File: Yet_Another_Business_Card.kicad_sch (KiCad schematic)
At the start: 415 parts, among them U1 STM32F103C8Tx

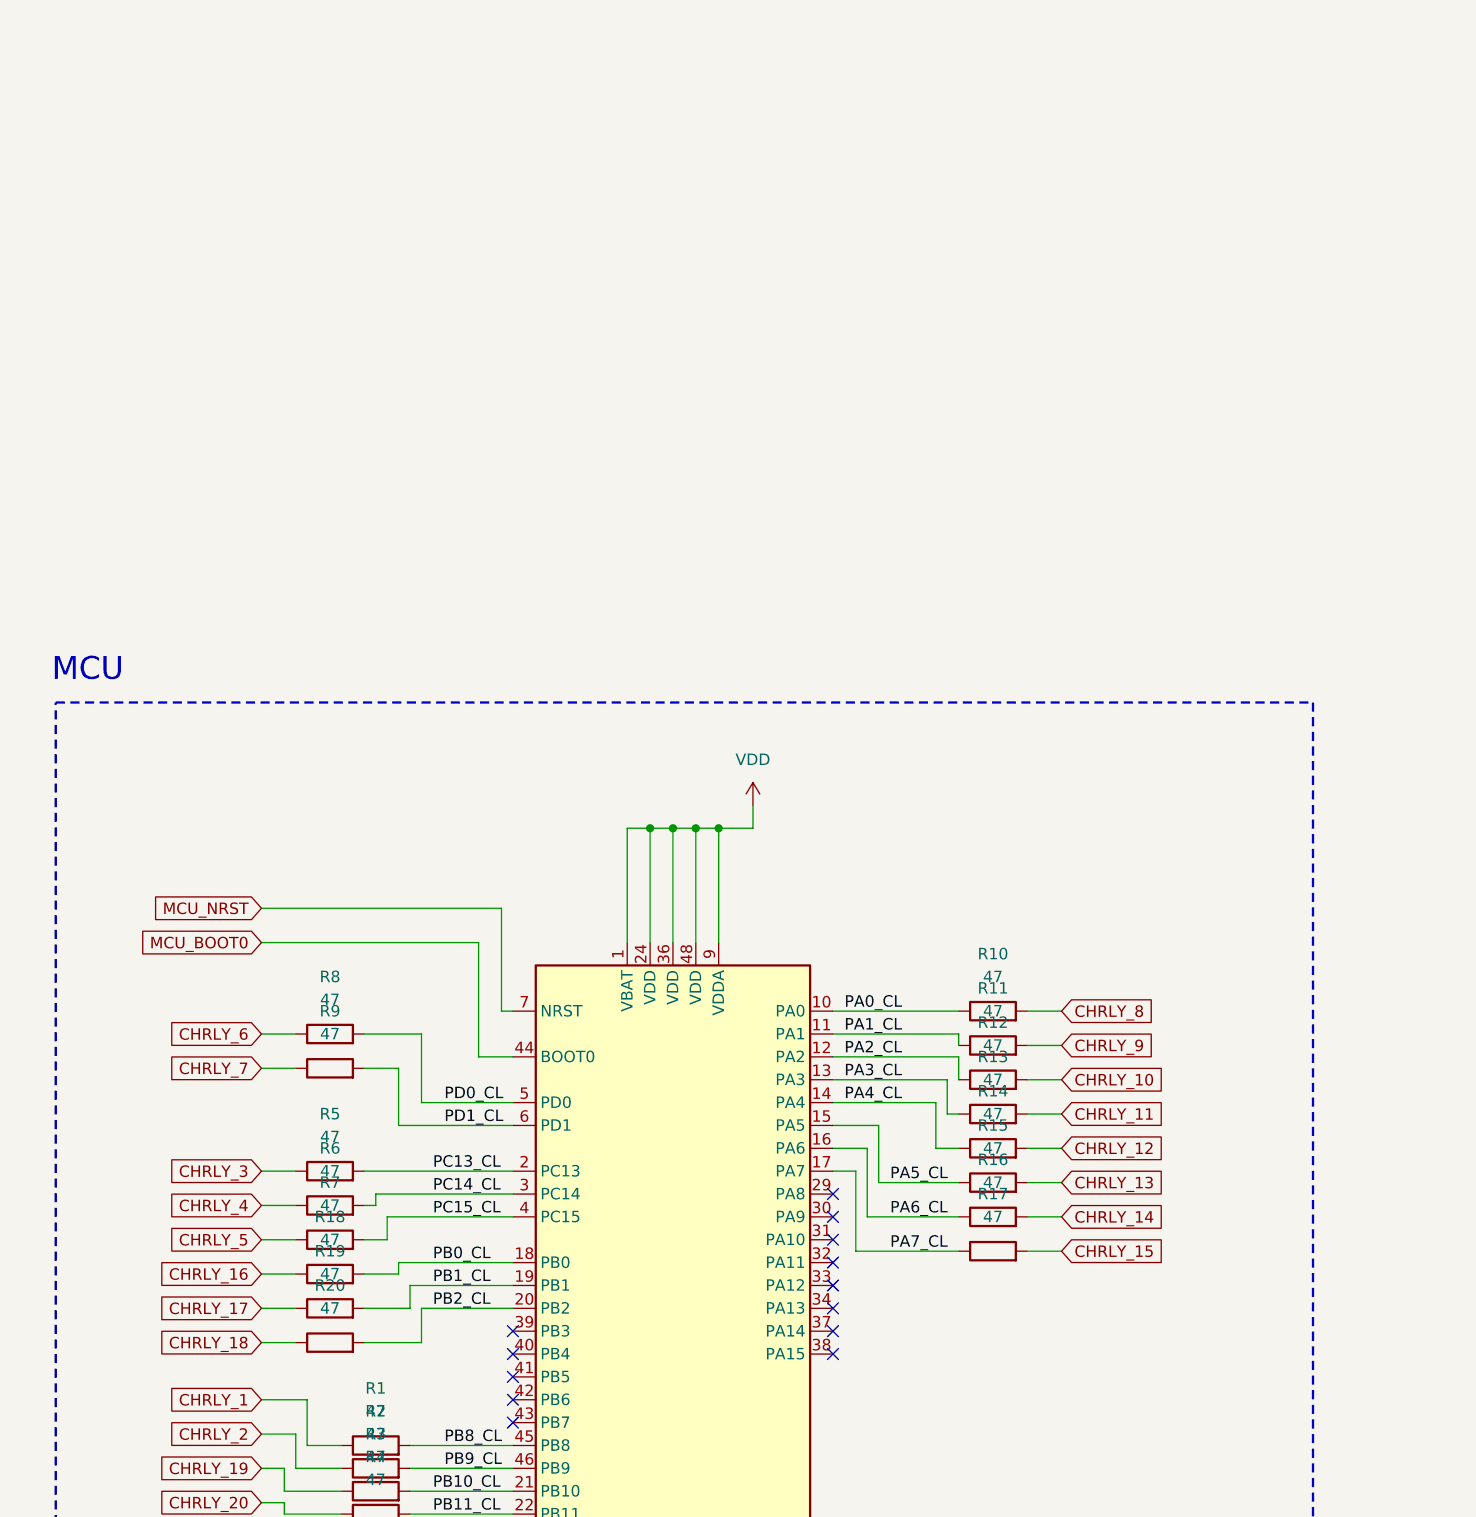
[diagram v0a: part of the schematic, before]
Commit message: Added SWDIO connector, python script to convert gif to matrix data
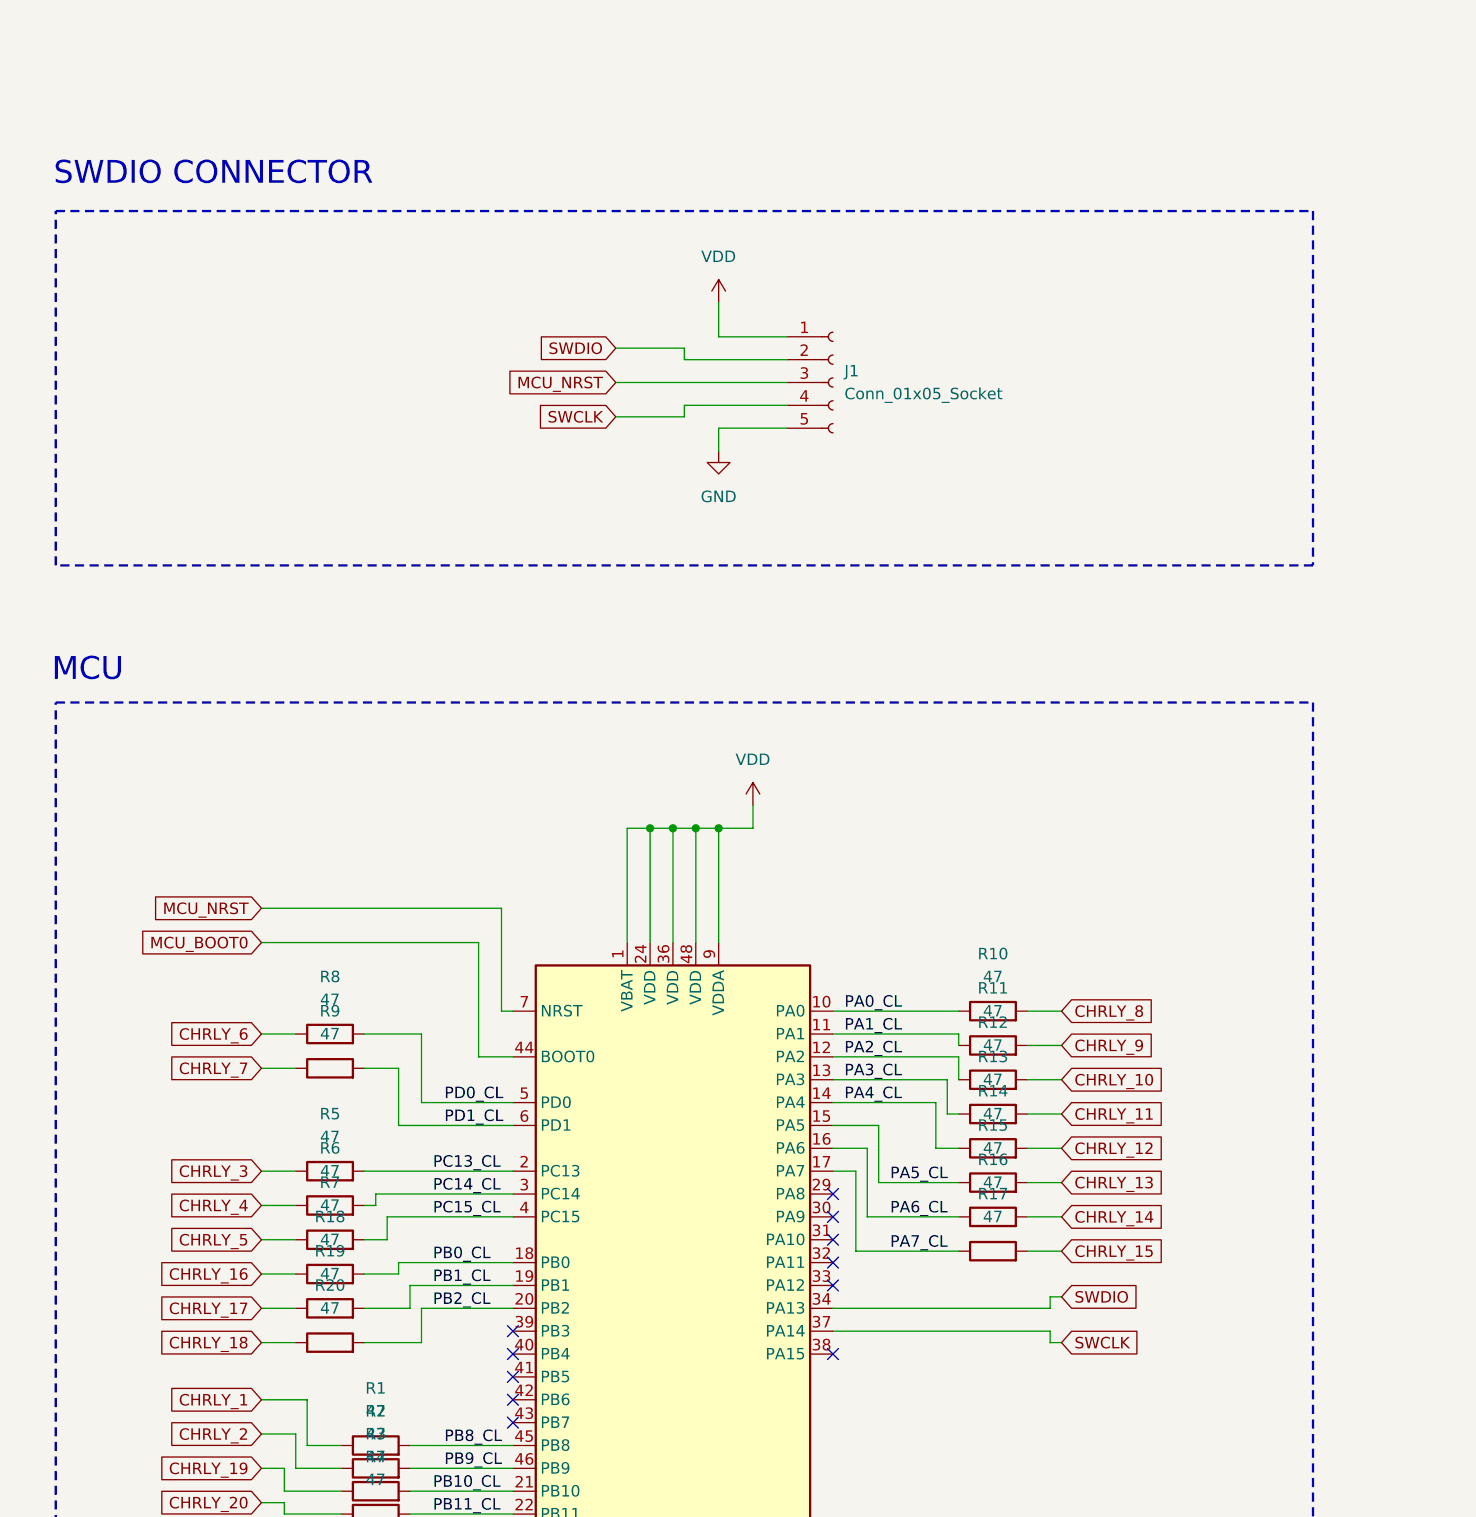
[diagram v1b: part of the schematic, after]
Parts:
- added J1: Conn_01x05_Socket, Connector_PinSocket_2.54mm:PinSocket_1x05_P2.54mm_Vertical, symbol Connector:Conn_01x05_Socket
- D10, D100, D101, D102, D103, D104, D105, D106, D107, D108, D109, D11, D110, D111, D112, D113, D114, D115, D116, D117, D118, D119, D12, D120, D121, D122, D123, D124, D125, D126, D127, D128, D129, D13, D130, D131, D132, D133, D134, D135, D136, D137, D138, D139, D14, D140, D141, D142, D143, D144, D145, D146, D147, D148, D149, D15, D150, D151, D152, D153, D154, D155, D156, D157, D158, D159, D16, D160, D161, D162, D163, D164, D165, D166, D167, D168, D169, D17, D170, D171, D172, D173, D174, D175, D176, D177, D178, D179, D18, D180, D181, D182, D183, D184, D185, D186, D187, D188, D189, D19, D190, D191, D192, D193, D194, D195, D196, D197, D198, D199, D2, D20, D200, D201, D202, D203, D204, D205, D206, D207, D208, D209, D21, D210, D211, D212, D213, D214, D215, D216, D217, D218, D219, D22, D220, D221, D222, D223, D224, D225, D226, D227, D228, D229, D23, D230, D231, D232, D233, D234, D235, D236, D237, D238, D239, D24, D240, D241, D242, D243, D244, D245, D246, D247, D248, D249, D25, D250, D251, D252, D253, D254, D255, D256, D257, D258, D259, D26, D260, D261, D262, D263, D264, D265, D266, D267, D268, D269, D27, D270, D271, D272, D273, D274, D275, D276, D277, D278, D279, D28, D280, D281, D282, D283, D284, D285, D286, D287, D288, D289, D29, D290, D291, D292, D293, D294, D295, D296, D297, D298, D299, D3, D30, D300, D301, D302, D303, D304, D305, D306, D307, D308, D309, D31, D310, D311, D312, D313, D314, D315, D316, D317, D318, D319, D32, D320, D321, D322, D323, D324, D325, D326, D327, D328, D329, D33, D330, D331, D332, D333, D334, D335, D336, D337, D338, D339, D34, D340, D341, D342, D343, D344, D345, D346, D347, D348, D349, D35, D350, D351, D352, D353, D354, D355, D356, D357, D358, D359, D36, D360, D361, D362, D363, D364, D365, D366, D367, D368, D369, D37, D370, D371, D372, D373, D374, D375, D376, D377, D378, D379, D38, D380, D381, D39, D4, D40, D41, D42, D43, D44, D45, D46, D47, D48, D49, D5, D50, D51, D52, D53, D54, D55, D56, D57, D58, D59, D6, D60, D61, D62, D63, D64, D65, D66, D67, D68, D69, D7, D70, D71, D72, D73, D74, D75, D76, D77, D78, D79, D8, D80, D81, D82, D83, D84, D85, D86, D87, D88, D89, D9, D90, D91, D92, D93, D94, D95, D96, D97, D98, D99: footprint LED_SMD:LED_0603_1608Metric -> Business_card_footprints:LED_0603_no_silkscreen
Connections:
- net GND: now also J1.5 (Pin_5)
- net MCU_NRST: now also J1.3 (Pin_3)
- net VDD: now also J1.1 (Pin_1)
- net SWDIO: now reaches U1.34 (PA13)
- net SWDIO: now also J1.2 (Pin_2)
- net SWCLK: now reaches U1.37 (PA14)
- net SWCLK: now also J1.4 (Pin_4)
- no-connect marks 16 -> 14
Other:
- note added: "SWDIO CONNECTOR"

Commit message: Updated firmware, PCB files are updated after the second prototype production (added just 2 battery holder footprints as a test)
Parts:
- removed BTN_DOWN1, BTN_DX1, BTN_SX1, BTN_UP1: SW_Push, Button_Switch_SMD:SW_Push_1P1T_XKB_TS-1187A, symbol Switch:SW_Push
- removed D115, D134, D153, D172, D191, D20, D210, D229, D248, D267, D286, D305, D324, D343, D362, D363, D364, D365, D366, D367, D368, D369, D370, D371, D372, D373, D374, D375, D376, D377, D378, D379, D380, D381, D39, D58, D77, D96: LED, Business_card_footprints:LED_0603_no_silkscreen, symbol Device:LED
- removed R12, R13, R14, R15, R17: 47, Resistor_SMD:R_0603_1608Metric, symbol Device:R
- added BTN_MAIN3, BTN_MAIN4, BTN_MAIN5: SW_Push, Button_Switch_SMD:SW_Push_1P1T_XKB_TS-1187A, symbol Switch:SW_Push
- added R18, R19, R20, R7: 47, Resistor_SMD:R_0603_1608Metric, symbol Device:R
- renumbered C6 to C1, C1 to C2, C2 to C3, C3 to C4, C4 to C5, C5 to C6, D2 to D1, D11 to D10, D106 to D100, D107 to D101, D108 to D102, D109 to D103, D110 to D104, D111 to D105, D112 to D106, D113 to D107, D114 to D108, D116 to D109, D12 to D11, D117 to D110, D118 to D111, D119 to D112, D120 to D113, D121 to D114, D122 to D115, D123 to D116, D124 to D117, D125 to D118, D126 to D119, D13 to D12, D127 to D120, D128 to D121, D129 to D122, D130 to D123, D131 to D124, D132 to D125, D133 to D126, D135 to D127, D136 to D128, D137 to D129, D14 to D13, D138 to D130, D139 to D131, D140 to D132, D141 to D133, D142 to D134, D143 to D135, D144 to D136, D145 to D137, D146 to D138, D147 to D139, D15 to D14, D148 to D140, D149 to D141, D150 to D142, D151 to D143, D152 to D144, D154 to D145, D155 to D146, D156 to D147, D157 to D148, D158 to D149, D16 to D15, D159 to D150, D160 to D151, D161 to D152, D162 to D153, D163 to D154, D164 to D155, D165 to D156, D166 to D157, D167 to D158, D168 to D159, D17 to D16, D169 to D160, D170 to D161, D171 to D162, D173 to D163, D174 to D164, D175 to D165, D176 to D166, D177 to D167, D178 to D168, D179 to D169, D18 to D17, D180 to D170, D181 to D171, D182 to D172, D183 to D173, D184 to D174, D185 to D175, D186 to D176, D187 to D177, D188 to D178, D189 to D179, D19 to D18, D190 to D180, D192 to D181, D193 to D182, D194 to D183, D195 to D184, D196 to D185, D197 to D186, D198 to D187, D199 to D188, D200 to D189, D21 to D19, D201 to D190, D202 to D191, D203 to D192, D204 to D193, D205 to D194, D206 to D195, D207 to D196, D208 to D197, D209 to D198, D211 to D199, D3 to D2, D22 to D20, D212 to D200, D213 to D201, D214 to D202, D215 to D203, D216 to D204, D217 to D205, D218 to D206, D219 to D207, D220 to D208, D221 to D209, D23 to D21, D222 to D210, D223 to D211, D224 to D212, D225 to D213, D226 to D214, D227 to D215, D228 to D216, D230 to D217, D231 to D218, D232 to D219, D24 to D22, D233 to D220, D234 to D221, D235 to D222, D236 to D223, D237 to D224, D238 to D225, D239 to D226, D240 to D227, D241 to D228, D242 to D229, D25 to D23, D243 to D230, D244 to D231, D245 to D232, D246 to D233, D247 to D234, D249 to D235, D250 to D236, D251 to D237, D252 to D238, D253 to D239, D26 to D24, D254 to D240, D255 to D241, D256 to D242, D257 to D243, D258 to D244, D259 to D245, D260 to D246, D261 to D247, D262 to D248, D263 to D249, D27 to D25, D264 to D250, D265 to D251, D266 to D252, D268 to D253, D269 to D254, D270 to D255, D271 to D256, D272 to D257, D273 to D258, D274 to D259, D28 to D26, D275 to D260, D276 to D261, D277 to D262, D278 to D263, D279 to D264, D280 to D265, D281 to D266, D282 to D267, D283 to D268, D284 to D269, D29 to D27, D285 to D270, D287 to D271, D288 to D272, D289 to D273, D290 to D274, D291 to D275, D292 to D276, D293 to D277, D294 to D278, D295 to D279, D30 to D28, D296 to D280, D297 to D281, D298 to D282, D299 to D283, D300 to D284, D301 to D285, D302 to D286, D303 to D287, D304 to D288, D306 to D289, D31 to D29, D307 to D290, D308 to D291, D309 to D292, D310 to D293, D311 to D294, D312 to D295, D313 to D296, D314 to D297, D315 to D298, D316 to D299, D4 to D3, D32 to D30, D317 to D300, D318 to D301, D319 to D302, D320 to D303, D321 to D304, D322 to D305, D323 to D306, D325 to D307, D326 to D308, D327 to D309, D33 to D31, D328 to D310, D329 to D311, D330 to D312, D331 to D313, D332 to D314, D333 to D315, D334 to D316, D335 to D317, D336 to D318, D337 to D319, D34 to D32, D338 to D320, D339 to D321, D340 to D322, D341 to D323, D342 to D324, D344 to D325, D345 to D326, D346 to D327, D347 to D328, D348 to D329, D35 to D33, D349 to D330, D350 to D331, D351 to D332, D352 to D333, D353 to D334, D354 to D335, D355 to D336, D356 to D337, D357 to D338, D358 to D339, D36 to D34, D359 to D340, D360 to D341, D361 to D342, D37 to D35, D38 to D36, D40 to D37, D41 to D38, D42 to D39, D5 to D4, D43 to D40, D44 to D41, D45 to D42, D46 to D43, D47 to D44, D48 to D45, D49 to D46, D50 to D47, D51 to D48, D52 to D49, D6 to D5, D53 to D50, D54 to D51, D55 to D52, D56 to D53, D57 to D54, D59 to D55, D60 to D56, D61 to D57, D62 to D58, D63 to D59, D7 to D6, D64 to D60, D65 to D61, D66 to D62, D67 to D63, D68 to D64, D69 to D65, D70 to D66, D71 to D67, D72 to D68, D73 to D69, D8 to D7, D74 to D70, D75 to D71, D76 to D72, D78 to D73, D79 to D74, D80 to D75, D81 to D76, D82 to D77, D83 to D78, D84 to D79, D9 to D8, D85 to D80, D86 to D81, D87 to D82, D88 to D83, D89 to D84, D90 to D85, D91 to D86, D92 to D87, D93 to D88, D94 to D89, D10 to D9, D95 to D90, D97 to D91, D98 to D92, D99 to D93, D100 to D94, D101 to D95, D102 to D96, D103 to D97, D104 to D98, D105 to D99, R5 to R1, R1 to R12, R2 to R13, R3 to R14, R4 to R15, R21 to R17, R6 to R2, R22 to R21, R7 to R3, R18 to R4, R19 to R5, R20 to R6
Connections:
- net CHRLY_20 is gone; now on net CHRLY_12: R15.1
- net PA2_CL is gone; now on net BTN_DOWN_PIN: U1.12 (PA2)
- net PA3_CL is gone; now on net BTN_UP_PIN: U1.13 (PA3)
- net PA4_CL is gone; now on net BTN_DX_PIN: U1.14 (PA4)
- net BTN_DOWN_PIN: now also BTN_MAIN5.2
- net BTN_DX_PIN: now also BTN_MAIN4.2
- net BTN_SX_PIN: now also U1.10 (PA0), U1.11 (PA1), BTN_MAIN3.2
- net BTN_UP_PIN: now also BTN_MAIN1.2
- net CHRLY_1: now also R4.1; no longer R12.1
- net CHRLY_10: now also R13.1
- net CHRLY_11: now also R14.1
- net CHRLY_13: now also R16.1
- net CHRLY_14: now also R18.1; no longer R16.2
- net CHRLY_15: now also R19.1
- net CHRLY_16: now also R20.1; no longer R4.1
- net CHRLY_17: now also R1.1; no longer R5.1
- net CHRLY_18: now also R2.1; no longer R6.1
- net CHRLY_19: now also R3.1; no longer R14.1
- net CHRLY_2: now also R5.1; no longer R13.1
- net CHRLY_3: now also R6.1; no longer R1.1
- net CHRLY_4: now also R7.1; no longer R2.1
- net CHRLY_5: now also R8.1; no longer R3.1
- net CHRLY_6: now also R9.1; no longer R8.1
- net CHRLY_7: now also R10.1; no longer R9.1
- net CHRLY_8: now also R11.1; no longer R10.2
- net CHRLY_9: now also R12.1; no longer R11.2
- net GND: no longer BTN_MAIN1.1
- net VDD: now also BTN_MAIN1.1, BTN_MAIN3.1, BTN_MAIN4.1, BTN_MAIN5.1
- net PB13_CL: now reaches U1.26 (PB13)
- net PB13_CL: now also R18.2
- net PB14_CL: now reaches U1.27 (PB14)
- net PB14_CL: now also R19.2
- net PB15_CL: now reaches U1.28 (PB15)
- net PB15_CL: now also R20.2
- net PB3_CL: now reaches U1.39 (PB3)
- net PB3_CL: now also R7.2
- net PB4_CL: now reaches U1.40 (PB4)
- net PB4_CL: now also R8.2
- net PB5_CL: now reaches U1.41 (PB5)
- net PB5_CL: now also R9.2
- net PB6_CL: now reaches U1.42 (PB6)
- net PB6_CL: now also R10.2
- net PB7_CL: now reaches U1.43 (PB7)
- net PB7_CL: now also R11.2
- net BTN_MAIN_PIN renamed PB12_CL
- net PB12_CL: now also R16.2; no longer BTN_MAIN1.2
- removed net PA0_CL: R10.1, U1.10 (PA0)
- removed net PA1_CL: R11.1, U1.11 (PA1)
- net PA5_CL: no longer names the net of U1.15 (PA5)
- net PA6_CL: no longer names the net of U1.16 (PA6)
- net PA6_CL: no longer R16.1
- net PA7_CL: no longer names the net of U1.17 (PA7)
- net PD0_CL: no longer names the net of U1.5 (PD0)
- net PD0_CL: no longer R8.2
- net PD1_CL: no longer names the net of U1.6 (PD1)
- net PD1_CL: no longer R9.2
- no-connect marks 14 -> 11
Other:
- moved on the sheet: R12, R13, R14, R15, R3, R4, R5, R6

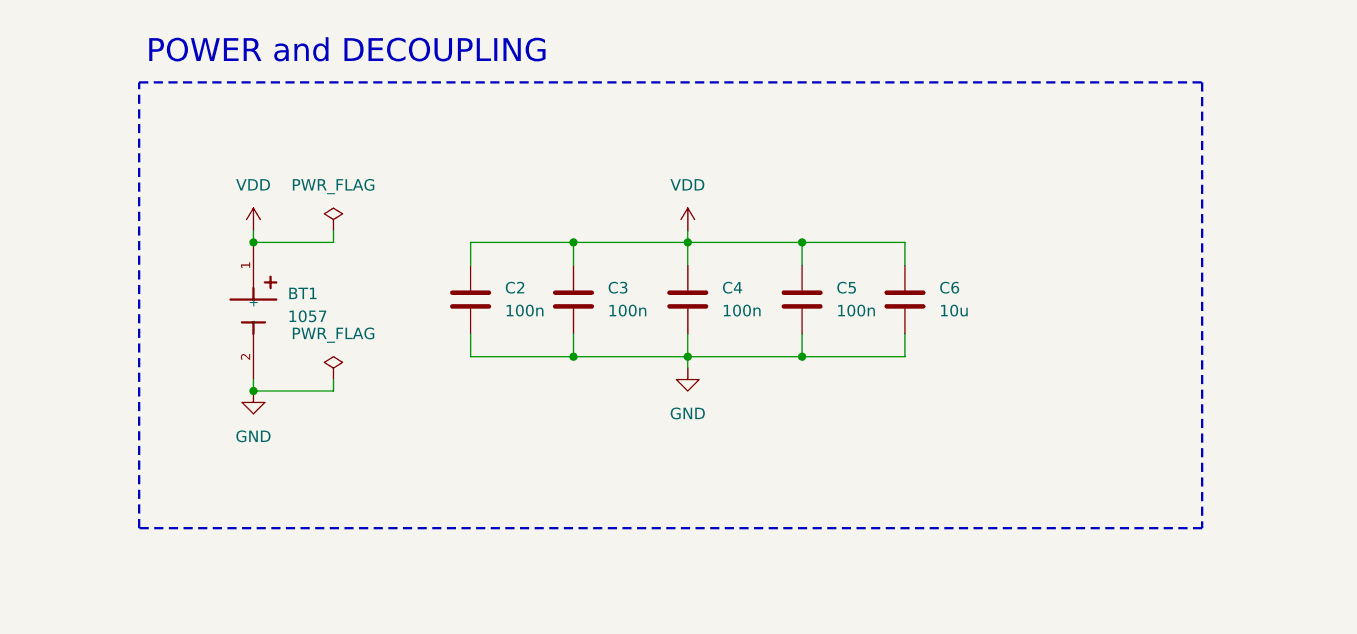
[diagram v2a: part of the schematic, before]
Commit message: Flashed code to second board of hw v2, ordered hw v3 boards
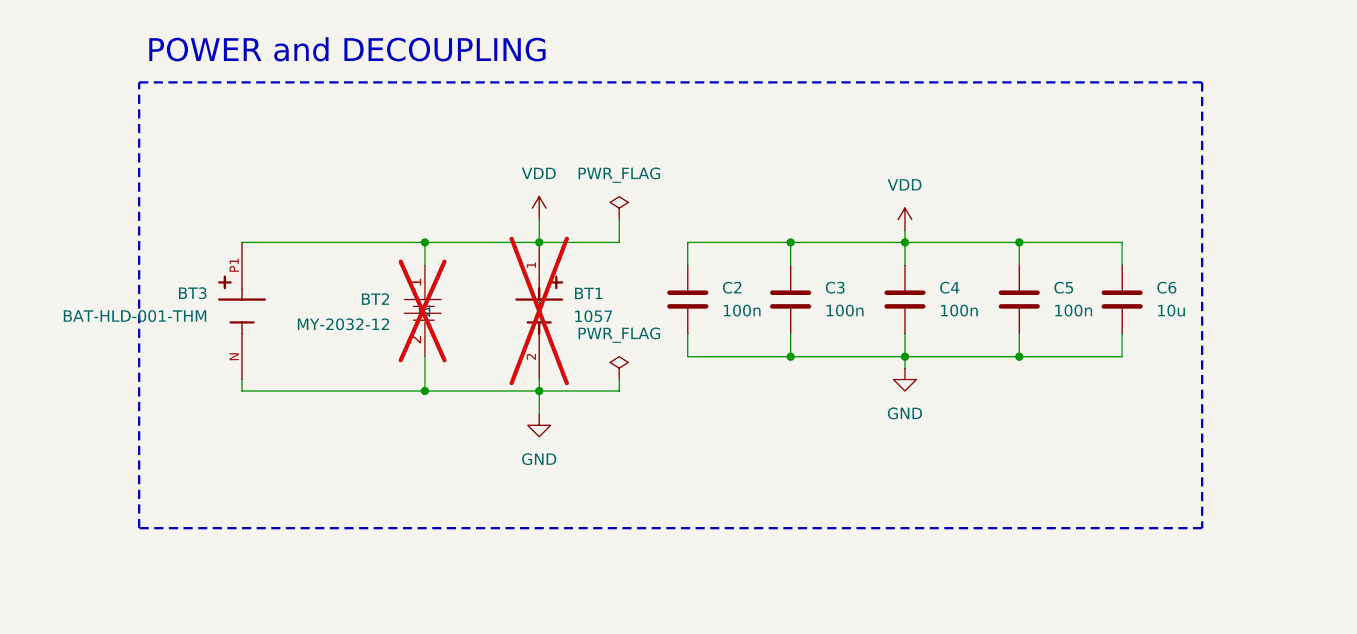
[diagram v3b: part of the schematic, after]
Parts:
- added BT2: MY-2032-12, easyeda2kicad:BAT-SMD_MY-2032-12, symbol easyeda2kicad:MY-2032-12
- added BT3: BAT-HLD-001-THM, Stratobotic_custom:BAT_BAT-HLD-001-THM, symbol Stratobotic_custom:BAT-HLD-001-THM
- BT1: now not fitted; now left out of the parts list
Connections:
- net GND: now also BT2.2, BT3.N
- net VDD: now also BT2.1, BT3.P1, BT3.P2, BT3.P3, BT3.P4
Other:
- moved on the sheet: C2, C3, C4, C5, C6
